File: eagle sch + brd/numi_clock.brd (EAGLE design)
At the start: 100 x 80 mm, 40 parts, among them IC1 MAX7219CWG, IC2 MEGA8-AI, IC4 DS1307Z, Q1 12 MHz, Q2 32kHz, X2 MINI-USB-UX60-MB-5S8

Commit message: Fixes #1
Fixes #1
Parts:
- removed C5, C6, C7, C8: 100nF, resistor:C0805
- removed C9: 27pF, resistor:C0805
- removed HC-SR505: (no value), con-lstb:MA03-1
- removed IC3: (no value), lm75:SO8_LM75
- removed IC4: DS1307Z, ds1307_pcf8583:SOIC8
- removed Q2: 32kHz, crystal:HC49U-V
- removed R12: 26k, resistor:M0805
- removed R15, R16: 10K, resistor:M0805
- removed SV3, SV4, SV5, SV6: (no value), con-lstb:MA09-1
- removed X2: MINI-USB-UX60-MB-5S8, con-hirose:UX60-MB-5S8
- added D2: 3.6V, SparkFun-DiscreteSemi:SOD-323
- added D3: red, SparkFun-LED:LED-1206
- added JP1: micro-usb, SparkFun-Connectors:USB-B-MICRO-SMD_V03
- added SV2: HC-SR505, con-lstb:MA03-1
- added U$1: MAX7219CWG, max7219:SO24L
- added U$2: DS1307SO8, SparkFun-FreqCtrl:SO08
- added U$3, U$4, U$5, U$6: IV-9, domestichacks:IV-9
- added Y1: 32.768kHz, SparkFun-FreqCtrl:TC26H
- C1: value 27pF -> 100nF; device resistor:C0805 -> rcl:C0805
- C2, C4: device resistor:C0805 -> rcl:C0805
- C3: value 100nF -> 27pF; device resistor:C0805 -> rcl:C0805
- D1: value RED -> 3.6V; device display-hp:HLMP6 -> SparkFun-DiscreteSemi:SOD-323
- IC1: value MAX7219CWG -> MEGA8-AI; device max7219:SO24L -> atmel:TQFP32-08
- IC2: value MEGA8-AI -> LM75; device atmel:TQFP32-08 -> lm75:SO8_LM75
- Q1: value 12 MHz -> 12MHz; device crystal:HC49U-V -> crystal:HC49/S
- R1, R2: device resistor:M0805 -> rcl:R0805
- R10, R8, R9: value 10K -> 10k; device resistor:M0805 -> rcl:R0805
- R11: value 10K -> 23k; device resistor:M0805 -> rcl:R0805
- R3: value 68 -> 1.8k; device resistor:M0805 -> rcl:R0805
- R4: value 1.8K -> 68; device resistor:M0805 -> rcl:R0805
- R5, R6: value 3v6 -> 10k; device e-halbleiter:Z-DIODE -> rcl:R0805
- R7: value 330 -> 10k; device resistor:M0805 -> rcl:R0805
- S1, S2: value SWITCH-MOMENTARY-2SMD -> SWITCH-MOMENTARY-2TACTILE-SWITCH-SMD-RIGHT-ANGLE; device SparkFun-Electromechanical:TACTILE-SWITCH-SMD -> SparkFun-Electromechanical:TACTILE_SWITCH-SMD-RIGHT-ANGLE
- SL1: value (none) -> VBATT
- SV1: value (none) -> SPI
- moved S1 44.7 mm to (-16.5, 55.9)
- moved R11 35.9 mm to (-16.5, 49.5)
- moved IC2 35.4 mm to (-50.8, 31.8)
- moved R9 29.0 mm to (-47.0, 49.5)
- moved R8 29.0 mm to (-41.9, 49.5)
- moved R5 21.7 mm to (-26.7, 49.5)
- moved IC1 21.6 mm to (-17.8, 20.3)
- moved R6 20.9 mm to (-31.8, 49.5)
- moved C2 20.8 mm to (-47.0, 41.9)
- moved R2 20.1 mm to (-52.1, 49.5)
- moved R3 19.1 mm to (-40.6, 41.9)
- moved Q1 17.1 mm to (-40.6, 31.8)
- moved R10 17.1 mm to (-58.4, 41.9)
- moved R7 16.2 mm to (-36.8, 49.5)
- moved R4 16.1 mm to (-57.1, 49.5)
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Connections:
- removed net CLK: IC1.13
- removed net N$12: R1.1
- removed net N$14: C9.1, IC3.8
- removed net N$15: IC2.4
- removed net N$16: R11.2
- removed net N$17: IC1.18, R12.2
- removed net N$18: IC2.8
- removed net N$19: IC2.7
- removed net N$20: IC2.1
- removed net N$21: R9.2
- removed net N$22: R8.1
- removed net N$23: R6.A
- removed net N$24: R5.C
- removed net N$26: R6.C
- removed net N$28: SL1.2
- removed net N$29: C2.1
- removed net N$30: D1.K, R7.1
- removed net N$31: SV1.2
- removed net N$32: R1.2
- removed net N$35: IC4.2, Q2.1
- removed net N$36: IC4.1, Q2.2
- removed net N$39: IC3.4
- removed net N$42: IC1.4, IC1.9
- removed net N$45: SV3.6
- removed net N$48: IC3.5
- removed net N$6: R2.1, X2.3
- new net N$10: IC1.1, R2.2
- new net N$8: D1.C, JP1.D-1, R2.1, R3.2
- net +3V3: now also R5.1, R6.1, R7.1, R9.1, S1.1, SL1.2, U$2.3; no longer IC4.3, R11.1, S2.1
- net +5V: now also D3.A, IC1.18, IC1.20, IC1.4, IC1.6, IC2.8, JP1.VBUS1, R1.2, R10.1, R11.1, R3.1, R8.1, SV1.2, SV2.1, U$1.19, U$2.8; no longer C3.2, C5.2, C6.2, C8.2, D1.A, IC1.19, IC2.18, IC2.20, IC2.6, IC4.8, R12.1, R15.1, R16.1, R4.1, X2.1
- net A: now also U$1.14, U$3.5, U$4.5, U$5.5, U$6.5; no longer IC1.14, SV3.8, SV4.8, SV5.8, SV6.8
- net B: now also U$1.16, U$3.3, U$4.3, U$5.3, U$6.3; no longer IC1.16, SV3.7, SV4.7, SV5.7, SV6.7
- net C: now also U$1.20, U$3.4, U$4.4, U$5.4, U$6.4; no longer IC1.20, SV4.6, SV5.6, SV6.6
- net CS: now also IC1.24, U$1.12; no longer IC1.12, IC2.24
- net D: now also U$1.23, U$3.8, U$4.8, U$5.8, U$6.8; no longer IC1.23, SV3.5, SV4.5, SV5.5, SV6.5
- net DIG0: now also R9.2, U$1.2, U$6.1; no longer IC1.2, SV3.9
- net DIG1: now also R7.2, U$1.11, U$5.1; no longer IC1.11
- net DIG2: now also R6.2, U$1.6, U$4.1; no longer IC1.6, SV5.9
- net DIG3: now also R5.2, U$1.7, U$3.1; no longer IC1.7, R8.2, SV6.9
- net DP: now also U$1.22, U$3.2, U$4.2, U$5.2, U$6.2; no longer IC1.22, SV3.1, SV4.1, SV5.1, SV6.1
- net E: now also U$1.21, U$3.9, U$4.9, U$5.9, U$6.9; no longer IC1.21, SV3.4, SV4.4, SV5.4, SV6.4
- net F: now also U$1.15, U$3.6, U$4.6, U$5.6, U$6.6; no longer IC1.15, SV3.3, SV4.3, SV5.3, SV6.3
- net G: now also U$1.17, U$3.7, U$4.7, U$5.7, U$6.7; no longer IC1.17, SV3.2, SV4.2, SV5.2, SV6.2
- net GND: now also C2.1, D1.A, D2.A, D3.C, IC1.21, IC1.3, IC1.5, IC2.4, IC2.6, IC2.7, JP1.GND1, JP1.ID1, S1.2, S2.2, SV2.3, U$1.4, U$1.9, U$2.4; no longer C5.1, C6.1, C7.1, C8.1, C9.2, HC-SR505.3, IC2.21, IC2.3, IC3.6, IC3.7, IC4.4, R5.A, R7.2, S1.3, S2.3
- net HC: now also IC1.23, SV2.2; no longer HC-SR505.2, IC2.23
- net MISO: now also IC1.16
- net MOSI: now also IC1.15, U$1.1; no longer IC1.1
- net N$1: now also C2.2, IC1.7; no longer C1.2
- net N$2: now also C3.2, IC1.8; no longer C2.2
- net N$3: now also R11.2, U$1.18; no longer HC-SR505.1
- net N$4: now also U$2.1, Y1.2; no longer R3.2
- net N$5: now also U$2.2, Y1.1; no longer S1.1
- net N$7: now also D2.C, JP1.D+1, R4.1; no longer R3.1, R4.2, X2.2
- net N$9: now also IC1.32, R4.2; no longer IC2.32, R2.2
- net RESET: now also C1.2, IC1.29, R1.1, S2.1; no longer C7.2, IC2.29
- net SCK: now also IC1.17, U$1.13
- net SCL: now also IC2.2, R10.2, U$2.6; no longer IC2.28, IC3.2, IC4.6, R16.2
- net SDA: now also IC2.1, R8.2, U$2.5; no longer IC2.27, IC3.1, IC4.5, R15.2

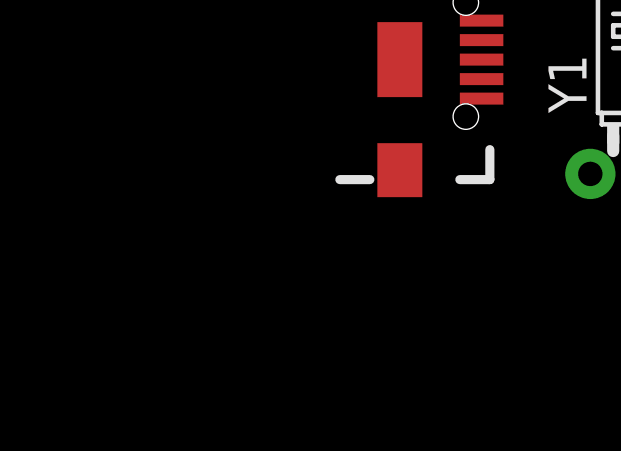
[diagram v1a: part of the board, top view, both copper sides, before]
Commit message: added buttons for hour, minute, function
added buttons for hour, minute, function
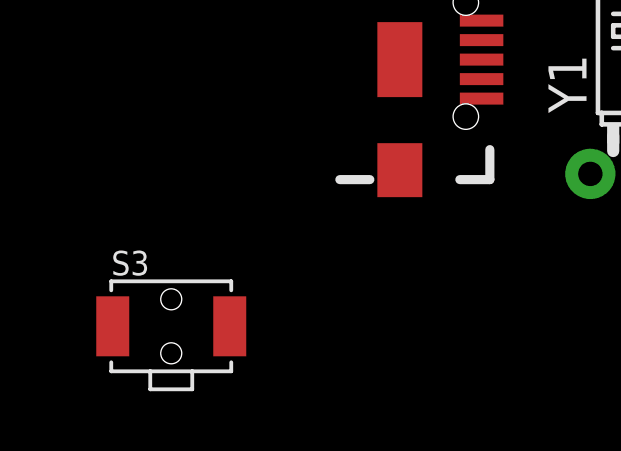
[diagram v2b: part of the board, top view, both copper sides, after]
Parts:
- added S3: SWITCH-MOMENTARY-2TACTILE-SWITCH-SMD-RIGHT-ANGLE, SparkFun-Electromechanical:TACTILE_SWITCH-SMD-RIGHT-ANGLE
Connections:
- new net FUNC: IC1.19, S3.1
- new net HOUR: IC1.25, S1.1
- new net MINUTE: IC1.26, S2.1
- net +3V3: no longer S1.1
- net GND: now also S3.2
- net RESET: no longer S2.1
- net SCL: now also IC1.28
- net SDA: now also IC1.27
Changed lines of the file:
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@@
 <attribute name="PROD_ID" value="XTAL-10112" x="-41.91" y="1.27" size="1.778" layer="27" display="off"/>
+</element>
+<element name="S3" library="SparkFun-Electromechanical" package="TACTILE_SWITCH-SMD-RIGHT-ANGLE" value="SWITCH-MOMENTARY-2TACTILE-SWITCH-SMD-RIGHT-ANGLE" x="-57.15" y="-3.81">
+<attribute name="PROD_ID" value="COMP-12265" x="-57.15" y="-3.81" size="1.778" layer="27" display="off"/>
 </element>
 </elements>
@@
 <contactref element="S1" pad="2"/>
 <contactref element="S2" pad="2"/>
-<wire x1="-46.805" y1="3.78" x2="-46.805" y2="4.43" width="0" layer="19" extent="1-1"/>
+<contactref element="S3" pad="2"/>
+<wire x1="-46.805" y1="3.78" x2="-55.2" y2="-3.81" width="0" layer="19" extent="1-1"/>
+<wire x1="-46.805" y1="4.43" x2="-46.805" y2="3.78" width="0" layer="19" extent="1-1"/>
 <wire x1="-31.115" y1="1.3208" x2="-46.805" y2="3.78" width="0" layer="19" extent="1-1"/>
 <wire x1="-24.765" y1="1.3208" x2="-31.115" y2="1.3208" width="0" layer="19" extent="1-1"/>
@@
 <signal name="RESET">
 <contactref element="SV1" pad="5"/>
-<contactref element="S2" pad="1"/>
 <contactref element="C1" pad="2"/>
 <contactref element="IC1" pad="29"/>
 <contactref element="R1" pad="1"/>
-<wire x1="-22.54" y1="49.53" x2="-24.81" y2="55.88" width="0" layer="19" extent="1-1"/>
 <wire x1="-26.99" y1="41.91" x2="-22.54" y2="49.53" width="0" layer="19" extent="1-1"/>
 <wire x1="-27.94" y1="30.48" x2="-26.99" y2="41.91" width="0" layer="19" extent="1-1"/>
@@
 <contactref element="U$2" pad="5"/>
 <contactref element="R8" pad="2"/>
+<contactref element="IC1" pad="27"/>
 <wire x1="-56.515" y1="33.0962" x2="-52.07" y2="28.575" width="0" layer="19" extent="1-1"/>
 <wire x1="-40.96" y1="49.53" x2="-56.515" y2="33.0962" width="0" layer="19" extent="1-1"/>
+<wire x1="-16.58" y1="24.6126" x2="-40.96" y2="49.53" width="0" layer="19" extent="1-1"/>
 </signal>
 <signal name="SCL">
@@
 <contactref element="U$2" pad="6"/>
 <contactref element="R10" pad="2"/>
+<contactref element="IC1" pad="28"/>
 <wire x1="-57.785" y1="33.0962" x2="-50.8" y2="28.575" width="0" layer="19" extent="1-1"/>
 <wire x1="-57.47" y1="41.91" x2="-57.785" y2="33.0962" width="0" layer="19" extent="1-1"/>
+<wire x1="-17.38" y1="24.6126" x2="-50.8" y2="28.575" width="0" layer="19" extent="1-1"/>
 </signal>
 <signal name="N$4">
@@
 <contactref element="R9" pad="1"/>
 <contactref element="SL1" pad="2"/>
-<contactref element="S1" pad="1"/>
 <contactref element="R6" pad="1"/>
-<wire x1="-27.62" y1="49.53" x2="-18.46" y2="55.88" width="0" layer="19" extent="1-1"/>
-<wire x1="-32.7" y1="49.53" x2="-27.62" y2="49.53" width="0" layer="19" extent="1-1"/>
-<wire x1="-37.78" y1="49.53" x2="-32.7" y2="49.53" width="0" layer="19" extent="1-1"/>
-<wire x1="-47.94" y1="49.53" x2="-37.78" y2="49.53" width="0" layer="19" extent="1-1"/>
-<wire x1="-57.785" y1="27.8638" x2="-47.94" y2="49.53" width="0" layer="19" extent="1-1"/>
+<wire x1="-47.94" y1="49.53" x2="-57.785" y2="27.8638" width="0" layer="19" extent="1-1"/>
+<wire x1="-37.78" y1="49.53" x2="-47.94" y2="49.53" width="0" layer="19" extent="1-1"/>
+<wire x1="-32.7" y1="49.53" x2="-37.78" y2="49.53" width="0" layer="19" extent="1-1"/>
+<wire x1="-27.62" y1="49.53" x2="-32.7" y2="49.53" width="0" layer="19" extent="1-1"/>
 <wire x1="-15.24" y1="3.81" x2="-27.62" y2="49.53" width="0" layer="19" extent="1-1"/>
 </signal>
@@
 <wire x1="-27.305" y1="11.3792" x2="-15.56" y2="49.53" width="0" layer="19" extent="1-1"/>
 </signal>
+<signal name="HOUR">
+<contactref element="S1" pad="1"/>
+<contactref element="IC1" pad="25"/>
+<wire x1="-14.98" y1="24.6126" x2="-18.46" y2="55.88" width="0" layer="19" extent="1-1"/>
+</signal>
+<signal name="FUNC">
+<contactref element="S3" pad="1"/>
+<contactref element="IC1" pad="19"/>
+<wire x1="-13.4874" y1="19.12" x2="-59.1" y2="-3.81" width="0" layer="19" extent="1-1"/>
+</signal>
+<signal name="MINUTE">
+<contactref element="S2" pad="1"/>
+<contactref element="IC1" pad="26"/>
+<wire x1="-15.78" y1="24.6126" x2="-24.81" y2="55.88" width="0" layer="19" extent="1-1"/>
+</signal>
 </signals>

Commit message: minor changes
minor changes
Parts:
- removed SL1: VBATT, con-amp-quick:02PA
- added BAT2: cr2032, SparkFun:BATTCOM_20MM_PTH
- added C5, C6, C7, C8: 100nF, rcl:C0805
- added D4: red, SparkFun-LED:LED-1206
- moved S3 133.3 mm to (75.9, 4.62)
- moved U$2 132.7 mm to (72.9, 49.6), turned to 180 degrees
- moved Y1 129.6 mm to (77.3, 52.0), turned to 270 degrees
- moved C4 129.0 mm to (90.9, 10.7), turned to 270 degrees
- moved R10 124.5 mm to (65.9, 47.3)
- moved SV1 123.1 mm to (92.3, 40.1), turned to 90 degrees
- moved SV2 117.4 mm to (95.2, 10.2), turned to 90 degrees
- moved R5 116.8 mm to (83.4, 10.4)
- moved U$3 111.8 mm to (82.5, 20.3)
- moved U$1 110.2 mm to (77.7, 37.7), turned to 180 degrees
- moved U$4 109.2 mm to (68.6, 20.3)
- moved R6 108.4 mm to (69.2, 10.2)
- moved IC2 107.3 mm to (52.8, 59.7)
- moved R8 107.3 mm to (65.3, 53.0)
- moved U$5 104.1 mm to (52.1, 20.3)
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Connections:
- removed net +3V3: R5.1, R6.1, R7.1, R9.1, SL1.2, U$2.3
- new net LED: D4.A, IC1.22
- new net N$6: BAT2.1, U$2.3
- net +5V: now also C5.2, C6.2, C7.2, C8.2, R5.1, R6.1, R7.1, R9.1
- net GND: now also BAT2.2, C5.1, C6.1, C7.1, C8.1, D4.C; no longer SL1.1
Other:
- board size 100 x 80 mm -> 100.8 x 69.8 mm

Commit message: layout adjustments
layout adjustments
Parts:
- removed R5, R6, R7: 10k, rcl:R0805
- removed U$3, U$4, U$5, U$6: IV-9, domestichacks:IV-9
- added C10, C9: 27pF, rcl:C0805
- added SV7: dig0, con-lstb:MA09-1
- added SV8: conn digits, con-lstb:MA04-1
- C2, C3: value 27pF -> 22pF
- Q1: device crystal:HC49/S -> crystal:CTS406
- moved R8 70.4 mm to (13.2, 5.62), flipped to the bottom, turned to 270 degrees
- moved R10 65.0 mm to (16.0, 5.62), flipped to the bottom, turned to 270 degrees
- moved Y1 63.9 mm to (22.6, 18.9), turned to 0 degrees
- moved U$2 63.3 mm to (23.2, 10.4), flipped to the bottom
- moved IC2 61.2 mm to (14.2, 12.2), flipped to the bottom, turned to 270 degrees
- moved D4 51.5 mm to (57.4, 9.81), flipped to the bottom, turned to 180 degrees
- moved SV1 48.4 mm to (62.7, 1.77), turned to 0 degrees
- moved D3 47.8 mm to (42.4, 2.50), flipped to the bottom, turned to 270 degrees
- moved R1 47.8 mm to (45.9, 3.38), flipped to the bottom, turned to 270 degrees
- moved R3 45.6 mm to (36.1, 11.6), flipped to the bottom, turned to 0 degrees
- moved C1 44.8 mm to (48.4, 3.38), flipped to the bottom, turned to 90 degrees
- moved SV2 42.6 mm to (53.1, 4.09), turned to 270 degrees
- moved R2 40.2 mm to (35.1, 14.8), flipped to the bottom, turned to 90 degrees
- moved C6 39.7 mm to (38.4, 8.88), flipped to the bottom, turned to 180 degrees
- moved D1 39.3 mm to (33.1, 12.6), flipped to the bottom
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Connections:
- net +5V: no longer R5.1, R6.1, R7.1
- net A: now also SV7.5; no longer U$3.5, U$4.5, U$5.5, U$6.5
- net B: now also SV7.3; no longer U$3.3, U$4.3, U$5.3, U$6.3
- net C: now also SV7.4; no longer U$3.4, U$4.4, U$5.4, U$6.4
- net D: now also SV7.8; no longer U$3.8, U$4.8, U$5.8, U$6.8
- net DIG0: now also SV7.1, SV8.1; no longer U$6.1
- net DIG1: now also SV8.2; no longer R7.2, U$5.1
- net DIG2: now also SV8.3; no longer R6.2, U$4.1
- net DIG3: now also SV8.4; no longer R5.2, U$3.1
- net DP: now also SV7.2; no longer U$3.2, U$4.2, U$5.2, U$6.2
- net E: now also SV7.9; no longer U$3.9, U$4.9, U$5.9, U$6.9
- net F: now also SV7.6; no longer U$3.6, U$4.6, U$5.6, U$6.6
- net G: now also SV7.7; no longer U$3.7, U$4.7, U$5.7, U$6.7
- net GND: now also C10.1, C9.1; no longer JP1.ID1
- net N$1: now also Q1.3; no longer Q1.2
- net N$4: now also C9.2, Y1.1; no longer Y1.2
- net N$5: now also C10.2, Y1.2; no longer Y1.1
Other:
- board size 100.8 x 69.8 mm -> 88.5 x 25.4 mm

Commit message: layout adjustments
layout adjustments
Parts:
- removed C6, C7, C8: 100nF, rcl:C0805
- removed D3, D4: red, SparkFun-LED:LED-1206
- removed R9: 10k, rcl:R0805
- removed SV1: SPI, con-lstb:MA03-2
- removed SV7: dig0, con-lstb:MA09-1
- added SV3: (no value), con-lstb:MA08-1
- moved S3 50.1 mm to (33.3, 13.1)
- moved R10 47.0 mm to (62.2, 14.2), turned to 90 degrees
- moved R8 46.3 mm to (56.9, 21.0), turned to 0 degrees
- moved IC2 43.1 mm to (57.2, 15.7), turned to 180 degrees
- moved S1 41.4 mm to (68.4, 12.9), turned to 180 degrees
- moved C4 30.9 mm to (56.1, 34.3), turned to 0 degrees
- moved SV2 30.8 mm to (50.2, 34.8), turned to 0 degrees
- moved U$2 27.3 mm to (50.2, 14.4), turned to 90 degrees
- moved C9 21.8 mm to (39.9, 12.8), turned to 180 degrees
- moved Y1 21.6 mm to (43.6, 13.9), turned to 90 degrees
- moved R3 18.0 mm to (31.8, 29.1), turned to 180 degrees
- moved D2 17.9 mm to (37.1, 29.4)
- moved C5 16.9 mm to (42.0, 23.1), turned to 90 degrees
- moved IC1 16.2 mm to (49.8, 26.8)
- moved BAT2 15.9 mm to (26.1, 33.8)
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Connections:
- removed net LED: D4.A, IC1.22
- removed net MISO: IC1.16, SV1.1
- new net AVCC: IC1.18
- net +5V: no longer C6.2, C7.2, C8.2, D3.A, IC1.18, R9.1, SV1.2
- net A: now also SV3.8; no longer SV7.5
- net B: now also SV3.7, U$1.15; no longer SV7.3, U$1.16
- net C: now also SV3.6, U$1.16; no longer SV7.4, U$1.20
- net D: now also SV3.5, U$1.17; no longer SV7.8, U$1.23
- net DIG0: no longer R9.2, SV7.1
- net DIG1: now also U$1.6; no longer U$1.11
- net DIG2: now also U$1.7; no longer U$1.6
- net DIG3: now also U$1.11; no longer U$1.7
- net DP: now also SV3.1, U$1.23; no longer SV7.2, U$1.22
- net E: now also SV3.4, U$1.20; no longer SV7.9, U$1.21
- net F: now also SV3.3, U$1.21; no longer SV7.6, U$1.15
- net FUNC: now also IC1.22; no longer IC1.19
- net G: now also SV3.2, U$1.22; no longer SV7.7, U$1.17
- net GND: no longer C6.1, C7.1, C8.1, D3.C, D4.C, SV1.6
- net HC: now also IC1.13; no longer IC1.23
- net HOUR: now also IC1.26; no longer IC1.25
- net MINUTE: now also IC1.25; no longer IC1.26
- net MOSI: no longer SV1.4
- net N$10: now also IC1.11; no longer IC1.1
- net RESET: no longer SV1.5
- net SCK: no longer SV1.3
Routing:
- net +5V: track 0.00 -> 226.0 mm, vias 0 -> 2
- net FUNC: track 0.00 -> 77.9 mm, vias 0 -> 3
- net N$10: track 0.00 -> 50.6 mm, vias 0 -> 4
- net MOSI: track 0.00 -> 37.9 mm
- net GND: track 0.00 -> 34.1 mm
- net MINUTE: track 0.00 -> 29.2 mm
- net N$6: track 0.00 -> 24.5 mm
- net HOUR: track 0.00 -> 24.3 mm
- net SCL: track 0.00 -> 22.5 mm
- net N$9: track 0.00 -> 20.2 mm
- net SDA: track 0.00 -> 14.8 mm
- net CS: track 0.00 -> 12.8 mm
- net SCK: track 0.00 -> 11.9 mm, vias 0 -> 2
- net N$8: track 0.00 -> 10.8 mm
- net N$3: track 0.00 -> 10.2 mm
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- added copper zone on layer 16, net GND
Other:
- board size 88.5 x 25.4 mm -> 71.4 x 28.4 mm

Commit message: later edit
later edit
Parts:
- moved R11 0.64 mm to (62.5, 28.3)
- moved C5 0.52 mm to (42.1, 23.6)
- moved R8 0.50 mm to (56.9, 21.5)
- moved S3 0.50 mm to (33.3, 12.6)
- moved C2 0.40 mm to (40.0, 23.5)
- moved C3 0.40 mm to (41.9, 33.5)
- moved Q1 0.25 mm to (41.1, 29.0)
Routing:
- net +5V: track 226.0 -> 208.1 mm
- net FUNC: track 77.9 -> 94.5 mm, vias 3 -> 4
- net SCL: track 22.5 -> 28.1 mm
- net GND: track 34.1 -> 38.7 mm
- net HOUR: track 24.3 -> 25.5 mm
- net CS: track 12.8 -> 11.9 mm
- net SDA: track 14.8 -> 15.3 mm
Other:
- board size 71.4 x 28.4 mm -> 71.2 x 30.1 mm

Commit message: routed all tracks
routed all tracks
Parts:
- added D3: (no value), sym:R0805
- moved C1 1.18 mm to (47.6, 18.6), turned to 0 degrees
- moved D1 1.07 mm to (32.8, 23.9), turned to 270 degrees
- moved R10 0.64 mm to (62.9, 14.1)
- moved R2 0.40 mm to (31.8, 26.8), turned to 0 degrees
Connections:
- new net LED: D3.1, IC1.19
- net GND: now also D3.2
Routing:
- net GND: track 38.7 -> 80.4 mm, vias 0 -> 8
- net +5V: track 208.1 -> 227.3 mm
- net N$10: track 50.6 -> 39.3 mm
- net HOUR: track 25.5 -> 22.0 mm
- net LED: track 0.00 -> 3.01 mm
- net N$8: track 10.8 -> 8.16 mm
- net FUNC: track 94.5 -> 93.2 mm
- net MINUTE: track 29.0 -> 28.0 mm
- net N$9: track 20.2 -> 21.1 mm
- net RESET: track 7.62 -> 8.24 mm
- net SCL: track 28.1 -> 27.6 mm
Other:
- board size 71.2 x 30.1 mm -> 70.8 x 29.5 mm
